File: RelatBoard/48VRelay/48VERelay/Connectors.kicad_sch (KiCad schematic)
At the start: 4 parts, among them J2 RJ45_Hanrun_HR911105A_Horizon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, J4 TC2050

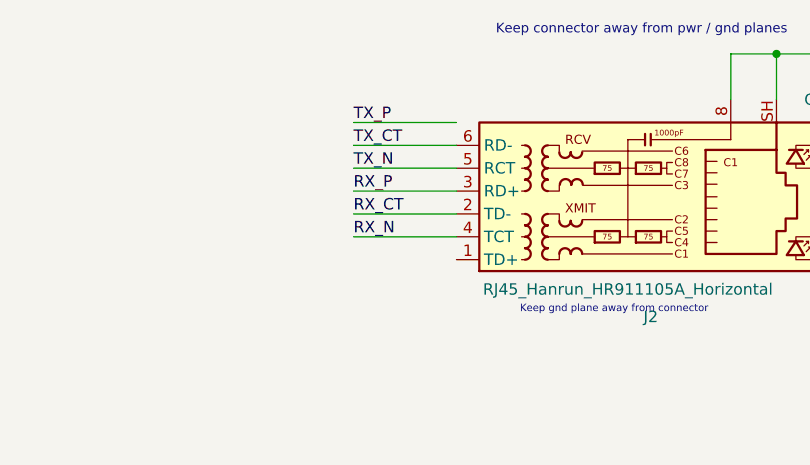
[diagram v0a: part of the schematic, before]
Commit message: update tx/rx eth routing
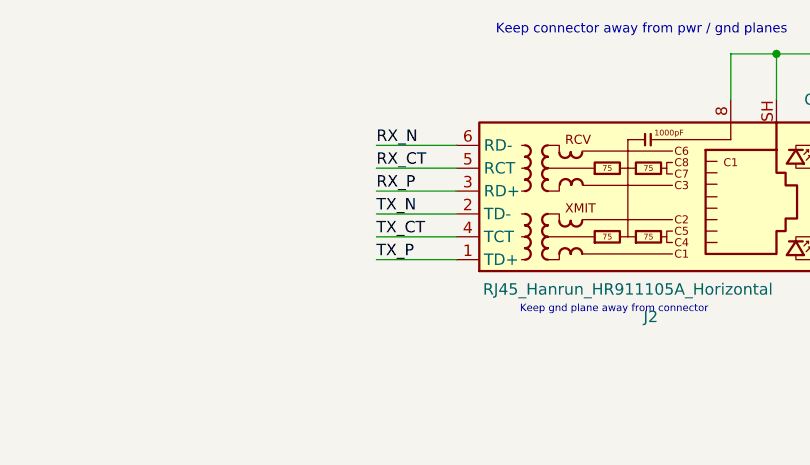
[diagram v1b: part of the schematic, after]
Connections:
- net RX_CT: now also J2.5 (RCT); no longer J2.2 (TD-)
- net RX_N: now also J2.6 (RD-); no longer J2.4 (TCT)
- net TX_CT: now also J2.4 (TCT); no longer J2.6 (RD-)
- net TX_N: now also J2.2 (TD-); no longer J2.5 (RCT)
- net TX_P: now also J2.1 (TD+)
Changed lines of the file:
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@@
 	(wire
 		(pts
-			(xy 173.99 58.42) (xy 162.56 58.42)
+			(xy 165.1 55.88) (xy 173.99 55.88)
 		)
 		(stroke
@@
 	(wire
 		(pts
-			(xy 162.56 50.8) (xy 173.99 50.8)
+			(xy 165.1 53.34) (xy 173.99 53.34)
 		)
 		(stroke
@@
 	(wire
 		(pts
-			(xy 237.49 63.5) (xy 237.49 62.23)
+			(xy 165.1 60.96) (xy 173.99 60.96)
 		)
 		(stroke
@@
 	(wire
 		(pts
-			(xy 162.56 55.88) (xy 173.99 55.88)
+			(xy 237.49 63.5) (xy 237.49 62.23)
 		)
 		(stroke
@@
 	(wire
 		(pts
+			(xy 165.1 63.5) (xy 173.99 63.5)
+		)
+		(stroke
+			(width 0)
+			(type default)
+		)
+	)
+	(wire
+		(pts
 			(xy 204.47 40.64) (xy 209.55 40.64)
 		)
@@
 	(wire
 		(pts
-			(xy 162.56 60.96) (xy 173.99 60.96)
+			(xy 165.1 58.42) (xy 173.99 58.42)
+		)
+		(stroke
+			(width 0)
+			(type default)
+		)
+	)
+	(wire
+		(pts
+			(xy 165.1 50.8) (xy 173.99 50.8)
 		)
 		(stroke
@@
 	(wire
 		(pts
-			(xy 173.99 53.34) (xy 162.56 53.34)
-		)
-		(stroke
-			(width 0)
-			(type default)
-		)
-	)
-	(wire
-		(pts
 			(xy 237.49 53.34) (xy 237.49 50.8)
 		)
@@
 		)
 	)
-	(wire
-		(pts
-			(xy 173.99 48.26) (xy 162.56 48.26)
-		)
-		(stroke
-			(width 0)
-			(type default)
-		)
-	)
-	(label "TX_CT"
-		(at 162.56 50.8 0)
+	(label "RX_CT"
+		(at 165.1 53.34 0)
 		(effects
 			(font
@@
 		)
 	)
-	(label "TX_N"
-		(at 162.56 53.34 0)
+	(label "RX_N"
+		(at 165.1 50.8 0)
 		(effects
 			(font
@@
 		)
 	)
-	(label "TX_P"
-		(at 162.56 48.26 0)
+	(label "TX_CT"
+		(at 165.1 60.96 0)
 		(effects
 			(font
@@
 		)
 	)
-	(label "RX_N"
-		(at 162.56 60.96 0)
+	(label "TX_P"
+		(at 165.1 63.5 0)
 		(effects
 			(font
@@
 	)
 	(label "RX_P"
-		(at 162.56 55.88 0)
+		(at 165.1 55.88 0)
 		(effects
 			(font
@@
 		)
 	)
-	(label "RX_CT"
-		(at 162.56 58.42 0)
+	(label "TX_N"
+		(at 165.1 58.42 0)
 		(effects
 			(font

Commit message: JTAG left
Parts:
- added J3: B4B-PH-SM4-TB, CONN_B4B-PH-SM4-TB_JST, symbol 2026-07-13_07-11-00:B4B-PH-SM4-TB
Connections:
- net GND: now also J3.4
- new net +3V3: J3.1
- new net UART_RXD: J3.3
- new net UART_TXD: J3.2

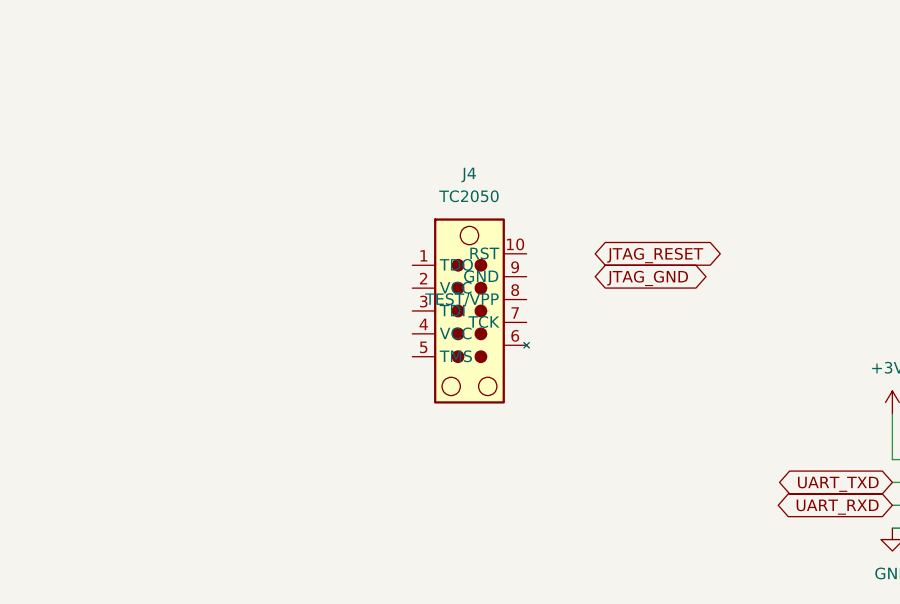
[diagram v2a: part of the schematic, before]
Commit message: update txrx routing length
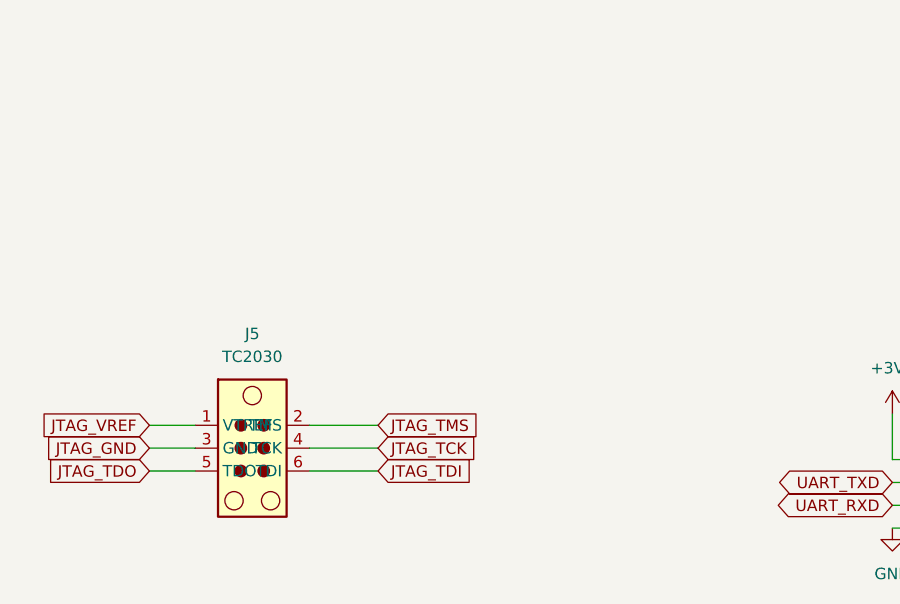
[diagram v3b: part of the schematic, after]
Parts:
- removed J4: TC2050, Connector:Tag-Connect_TC2050-IDC-NL_2x05_P1.27mm_Vertical, symbol Connector:TC2050
- added J5: TC2030, Connector:Tag-Connect_TC2030-IDC-NL_2x03_P1.27mm_Vertical, symbol Connector:TC2030
- J3: footprint CONN_B4B-PH-SM4-TB_JST -> Connector_PinHeader_2.54mm:PinHeader_1x04_P2.54mm_Vertical
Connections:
- net JTAG_GND: now also J5.3 (GND)
- new net JTAG_TCK: J5.4 (TCK)
- new net JTAG_TDI: J5.6 (TDI)
- new net JTAG_TDO: J5.5 (TDO)
- new net JTAG_TMS: J5.2 (TMS)
- new net JTAG_VREF: J5.1 (VTREF)
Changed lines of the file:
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@@
+	(wire
+		(pts
+			(xy 54.61 97.79) (xy 59.69 97.79)
+		)
+		(stroke
+			(width 0)
+			(type default)
+		)
+	)
 	(wire
 		(pts
@@
 	(wire
 		(pts
+			(xy 54.61 102.87) (xy 59.69 102.87)
+		)
+		(stroke
+			(width 0)
+			(type default)
+		)
+	)
+	(wire
+		(pts
 			(xy 137.16 101.6) (xy 143.51 101.6)
 		)
@@
 	(wire
 		(pts
+			(xy 54.61 100.33) (xy 59.69 100.33)
+		)
+		(stroke
+			(width 0)
+			(type default)
+		)
+	)
+	(wire
+		(pts
 			(xy 217.17 50.8) (xy 224.79 50.8)
 		)
@@
 	(wire
 		(pts
+			(xy 72.39 102.87) (xy 80.01 102.87)
+		)
+		(stroke
+			(width 0)
+			(type default)
+		)
+	)
+	(wire
+		(pts
 			(xy 204.47 40.64) (xy 209.55 40.64)
 		)
@@
 	(wire
 		(pts
+			(xy 72.39 100.33) (xy 80.01 100.33)
+		)
+		(stroke
+			(width 0)
+			(type default)
+		)
+	)
+	(wire
+		(pts
+			(xy 72.39 97.79) (xy 80.01 97.79)
+		)
+		(stroke
+			(width 0)
+			(type default)
+		)
+	)
+	(wire
+		(pts
 			(xy 209.55 40.64) (xy 214.63 40.64)
 		)
@@
 			(width 0)
 			(type default)
+		)
+	)
+	(global_label "JTAG_TMS"
+		(shape input)
+		(at 80.01 97.79 0)
+		(fields_autoplaced yes)
+		(effects
+			(font
+				(size 1.27 1.27)
+			)
+			(justify left)
+		)
+		(property "Intersheetrefs" "${INTERSHEET_REFS}"
+			(at 91.8851 97.79 0)
+			(hide yes)
+			(show_name no)
+			(do_not_autoplace no)
+			(effects
+				(font
+					(size 1.27 1.27)
+				)
+				(justify left)
+			)
+		)
+	)
+	(global_label "JTAG_TDI"
+		(shape input)
+		(at 80.01 102.87 0)
+		(fields_autoplaced yes)
+		(effects
+			(font
+				(size 1.27 1.27)
+			)
+			(justify left)
+		)
+		(property "Intersheetrefs" "${INTERSHEET_REFS}"
+			(at 91.099 102.87 0)
+			(hide yes)
+			(show_name no)
+			(do_not_autoplace no)
+			(effects
+				(font
+					(size 1.27 1.27)
+				)
+				(justify left)
+			)
+		)
+	)
+	(global_label "JTAG_GND"
+		(shape input)
+		(at 54.61 100.33 180)
+		(fields_autoplaced yes)
+		(effects
+			(font
+				(size 1.27 1.27)
+			)
+			(justify right)
+		)
+		(property "Intersheetrefs" "${INTERSHEET_REFS}"
+			(at 42.4929 100.33 0)
+			(hide yes)
+			(show_name no)
+			(do_not_autoplace no)
+			(effects
+				(font
+					(size 1.27 1.27)
+				)
+				(justify right)
+			)
+		)
+	)
+	(global_label "JTAG_VREF"
+		(shape input)
+		(at 54.61 97.79 180)
+		(fields_autoplaced yes)
+		(effects
+			(font
+				(size 1.27 1.27)
+			)
+			(justify right)
+		)
+		(property "Intersheetrefs" "${INTERSHEET_REFS}"
+			(at 41.7672 97.79 0)
+			(hide yes)
+			(show_name no)
+			(do_not_autoplace no)
+			(effects
+				(font
+					(size 1.27 1.27)
+				)
+				(justify right)
+			)
 		)
 	)
@@
 		)
 	)
-	(global_label "JTAG_GND"
-		(shape bidirectional)
-		(at 104.14 81.28 0)
-		(fields_autoplaced yes)
-		(effects
-			(font
-				(size 1.27 1.27)
-			)
-			(justify left)
-		)
-		(property "Intersheetrefs" "${INTERSHEET_REFS}"
-			(at 117.3684 81.28 0)
-			(hide yes)
-			(show_name no)
-			(do_not_autoplace no)
-			(effects
-				(font
-					(size 1.27 1.27)
-				)
-				(justify left)
-			)
-		)
-	)
 	(global_label "UART_RXD"
 		(shape bidirectional)
@@
 		)
 	)
+	(global_label "JTAG_TCK"
+		(shape input)
+		(at 80.01 100.33 0)
+		(fields_autoplaced yes)
+		(effects
+			(font
+				(size 1.27 1.27)
+			)
+			(justify left)
+		)
+		(property "Intersheetrefs" "${INTERSHEET_REFS}"
+			(at 91.7642 100.33 0)
+			(hide yes)
+			(show_name no)
+			(do_not_autoplace no)
+			(effects
+				(font
+					(size 1.27 1.27)
+				)
+				(justify left)
+			)
+		)
+	)
 	(global_label "TX_P"
 		(shape bidirectional)
@@
 		)
 	)
+	(global_label "JTAG_TDO"
+		(shape input)
+		(at 54.61 102.87 180)
+		(fields_autoplaced yes)
+		(effects
+			(font
+				(size 1.27 1.27)
+			)
+			(justify right)
+		)
+		(property "Intersheetrefs" "${INTERSHEET_REFS}"
+			(at 42.7953 102.87 0)
+			(hide yes)
+			(show_name no)
+			(do_not_autoplace no)
+			(effects
+				(font
+					(size 1.27 1.27)
+				)
+				(justify right)
+			)
+		)
+	)
 	(global_label "LINK_LED"
 		(shape bidirectional)
@@
 		)
 	)
-	(global_label "JTAG_RESET"
-		(shape bidirectional)
-		(at 104.14 78.74 0)
-		(fields_autoplaced yes)
-		(effects
-			(font
-				(size 1.27 1.27)
-			)
-			(justify left)
-		)
-		(property "Intersheetrefs" "${INTERSHEET_REFS}"
-			(at 119.243 78.74 0)
-			(hide yes)
-			(show_name no)
-			(do_not_autoplace no)
-			(effects
-				(font
-					(size 1.27 1.27)
-				)
-				(justify left)
+	(symbol
+		(lib_name "TC2030_1")
+		(lib_id "Connector:TC2030")
+		(at 64.77 100.33 0)
+		(unit 1)
+		(body_style 1)
+		(exclude_from_sim no)
+		(in_bom no)
+		(on_board yes)
+		(in_pos_files yes)
+		(dnp no)
+		(fields_autoplaced yes)
+		(property "Reference" "J5"
+			(at 66.04 87.63 0)
+			(show_name no)
+			(do_not_autoplace no)
+			(effects
+				(font
+					(size 1.27 1.27)
+				)
+			)
+		)
+		(property "Value" "TC2030"
+			(at 66.04 90.17 0)
+			(show_name no)
+			(do_not_autoplace no)
+			(effects
+				(font
+					(size 1.27 1.27)
+				)
+			)
+		)
+		(property "Footprint" "Connector:Tag-Connect_TC2030-IDC-NL_2x03_P1.27mm_Vertical"
+			(at 62.484 112.014 0)
+			(hide yes)
+			(show_name no)
+			(do_not_autoplace no)
+			(effects
+				(font
+					(size 1.27 1.27)
+				)
+			)
+		)
+		(property "Datasheet" "https://www.tag-connect.com/wp-content/uploads/bsk-pdf-manager/2019/12/TC2030-IDC-NL-Datasheet-Rev-B.pdf"
+			(at 62.23 111.506 0)
+			(hide yes)
+			(show_name no)
+			(do_not_autoplace no)
+			(effects
+				(font
+					(size 1.27 1.27)
+				)
+			)
+		)
+		(property "Description" "Tag-Connect’s 6-pins connector"
+			(at 65.278 111.506 0)
+			(hide yes)
+			(show_name no)
+			(do_not_autoplace no)
+			(effects
+				(font
+					(size 1.27 1.27)
+				)
+			)
+		)
+		(pin "1"
+		)
+		(pin "6"
+		)
+		(pin "5"
+		)
+		(pin "2"
+		)
+		(pin "4"
+		)
+		(pin "3"
+		)
+		(instances
+			(project "48VERelay"
+				(path "/2d740e7a-a48e-41b8-b74e-ca0ab277f7d9/4e215b4b-7e65-4a7a-bed3-9a0c470bfd52"
+					(reference "J5")
+					(unit 1)
+				)
 			)
 		)
@@
 			)
 		)
-		(property "Footprint" "CONN_B4B-PH-SM4-TB_JST"
+		(property "Footprint" "Connector_PinHeader_2.54mm:PinHeader_1x04_P2.54mm_Vertical"
 			(at 143.51 101.6 0)
 			(hide yes)
@@
 					(unit 1)
 				)
-			)
-		)
-	)
-	(symbol
-		(lib_name "TC2050_1")
-		(lib_id "Connector:TC2050")
-		(at 88.9 85.09 0)
-		(unit 1)
-		(body_style 1)
-		(exclude_from_sim no)
-		(in_bom no)
-		(on_board yes)
-		(in_pos_files yes)
-		(dnp no)
-		(fields_autoplaced yes)
-		(property "Reference" "J4"
-			(at 90.17 69.85 0)
-			(show_name no)
-			(do_not_autoplace no)
-			(effects
-				(font
-					(size 1.27 1.27)
-				)
-			)
-		)
-		(property "Value" "TC2050"
-			(at 90.17 72.39 0)
-			(show_name no)
-			(do_not_autoplace no)
-			(effects
-				(font
-					(size 1.27 1.27)
-				)
-			)
-		)
-		(property "Footprint" "Connector:Tag-Connect_TC2050-IDC-NL_2x05_P1.27mm_Vertical"
-			(at 90.17 85.09 0)
-			(hide yes)
-			(show_name no)
-			(do_not_autoplace no)
-			(effects
-				(font
-					(size 1.27 1.27)
-				)
-			)
-		)
-		(property "Datasheet" "https://www.tag-connect.com/wp-content/uploads/bsk-pdf-manager/TC2050-IDC-NL_Datasheet_8.pdf"
-			(at 90.17 85.09 0)
-			(hide yes)
-			(show_name no)
-			(do_not_autoplace no)
-			(effects
-				(font
-					(size 1.27 1.27)
-				)
-			)
-		)
-		(property "Description" "Tag-Connect’s 10-pins connector"
-			(at 88.9 85.09 0)
-			(hide yes)
-			(show_name no)
-			(do_not_autoplace no)
-			(effects
-				(font
-					(size 1.27 1.27)
-				)
-			)
-		)
-		(pin "1"
-		)
-		(pin "2"
-		)
-		(pin "3"
-		)
-		(pin "4"
-		)
-		(pin "5"
-		)
-		(pin "6"
-		)
-		(pin "7"
-		)
-		(pin "8"
-		)
-		(pin "9"
-		)
-		(pin "10"
-		)
-		(instances
-			(project "48VERelay"
-				(path "/2d740e7a-a48e-41b8-b74e-ca0ab277f7d9/4e215b4b-7e65-4a7a-bed3-9a0c470bfd52"
-					(reference "J4")
-					(unit 1)
-				)

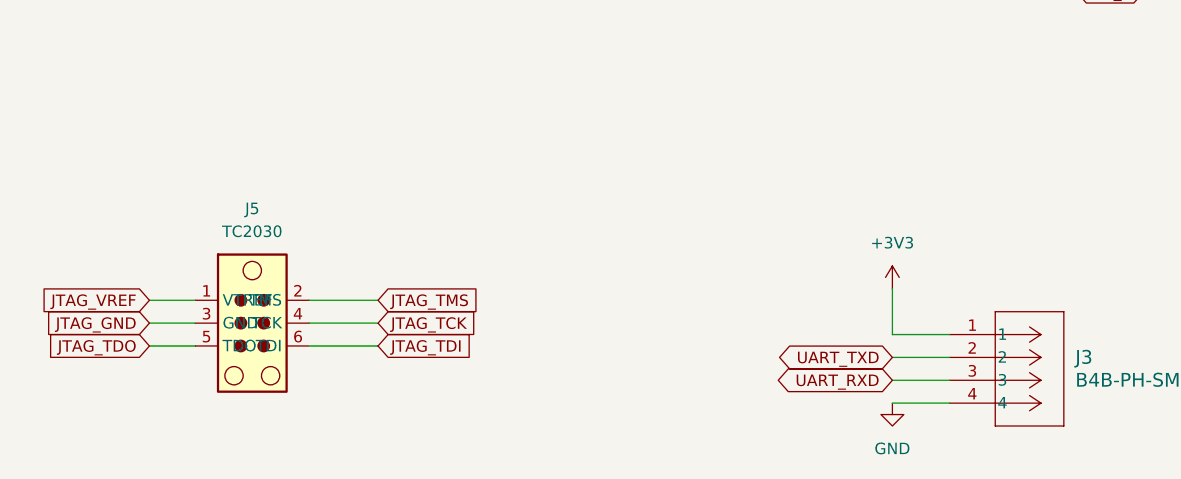
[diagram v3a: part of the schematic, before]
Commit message: wired uart and jtag
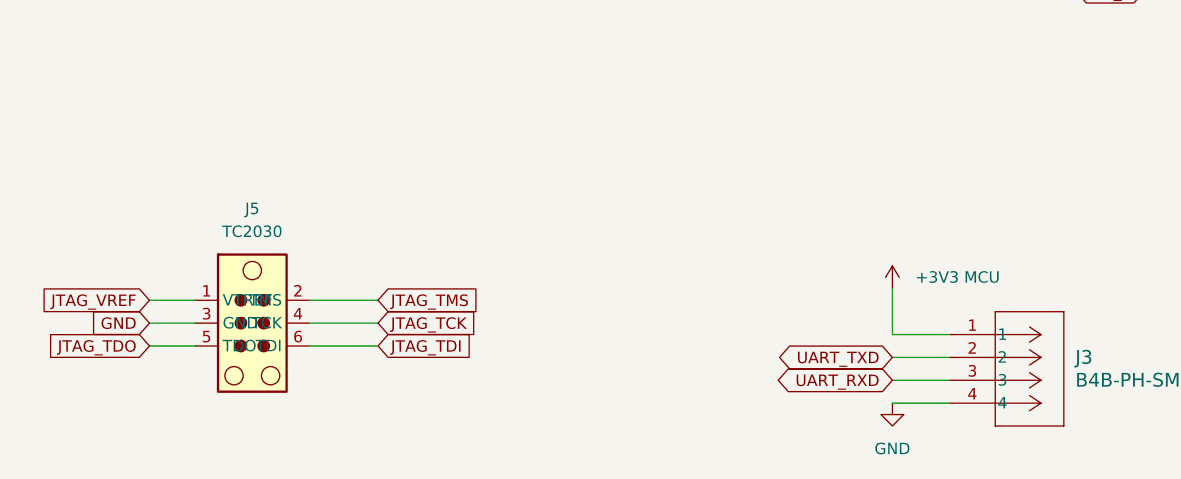
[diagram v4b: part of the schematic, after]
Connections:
- net JTAG_GND is gone; now on net GND: J5.3 (GND)
- net +3V3 renamed +3V3 MCU
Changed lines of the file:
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@@
 		)
 	)
-	(global_label "JTAG_GND"
+	(global_label "GND"
 		(shape input)
 		(at 54.61 100.33 180)
@@
 		)
 		(property "Intersheetrefs" "${INTERSHEET_REFS}"
-			(at 42.4929 100.33 0)
+			(at 47.7543 100.33 0)
 			(hide yes)
 			(show_name no)
@@
 			)
 		)
-		(property "Value" "+3V3"
-			(at 137.16 91.44 0)
-			(show_name no)
-			(do_not_autoplace no)
-			(effects
-				(font
-					(size 1.27 1.27)
-				)
-			)
-		)
+		(property "Value" "+3V3 MCU"
+			(at 139.7 95.2499 0)
+			(show_name no)
+			(do_not_autoplace no)
+			(effects
+				(font
+					(size 1.27 1.27)
+				)
+				(justify left)
+			)
+		)

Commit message: Final design
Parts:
- removed J5: TC2030, Connector:Tag-Connect_TC2030-IDC-NL_2x03_P1.27mm_Vertical, symbol Connector:TC2030
- added J4: TC2050, Connector:Tag-Connect_TC2050-IDC-NL_2x05_P1.27mm_Vertical, symbol Connector:TC2050
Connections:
- net GND: now also J4.2, J4.3, J4.4, J4.5
- net JTAG_TCK: now also J4.9
- net JTAG_TDI: now also J4.7
- net JTAG_TDO: now also J4.8
- net JTAG_TMS: now also J4.10
- net JTAG_VREF: now also J4.1
- no-connect marks 0 -> 1
